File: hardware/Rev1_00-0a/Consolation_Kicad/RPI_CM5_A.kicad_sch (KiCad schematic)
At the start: 61 parts, among them J17 61300311121, J19 RPI_CMx_A, J7 2998TR, Q17 2N7002, Q19 SSM3K56FS,LF, Q20 SSM3K56FS,LF, Q21 SSM3K56FS,LF, Q22 SSM3K56FS,LF, U19 SN74LVC1G125DBVR, U21 MCP7940NT-I/MS, Y2 32.768kHz

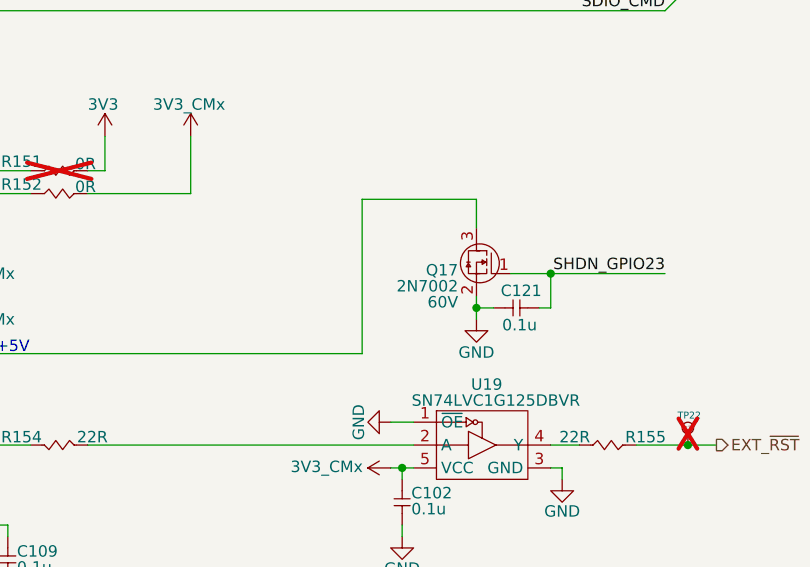
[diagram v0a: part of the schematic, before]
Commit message: Removed unnecessary functions (USB2 mux, CapTouch) Adjusted 220uF alum capacitor for codec (slimmer version)
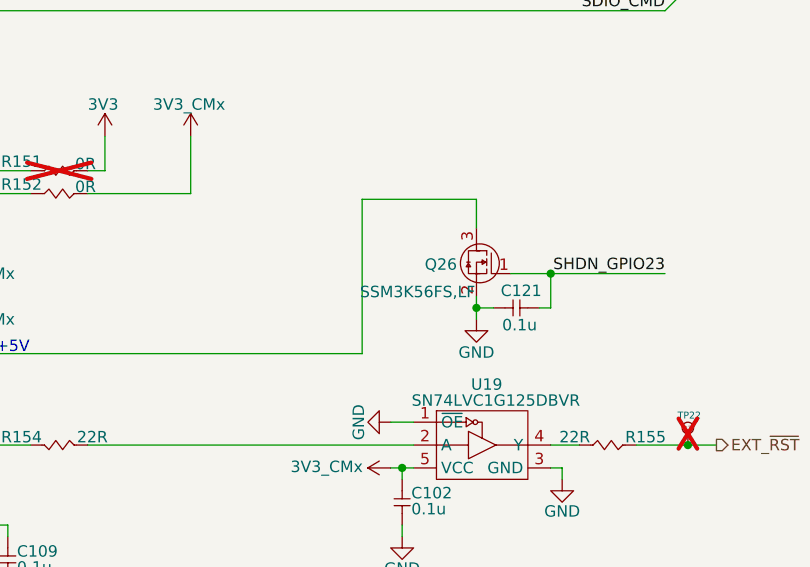
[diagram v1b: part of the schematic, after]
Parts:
- removed Q17: 2N7002, footprint:SOT-23-3, symbol KicadCompDb:Mosfet/MOSFET_00001
- added Q26: SSM3K56FS,LF, footprint:SC-75, symbol KicadCompDb:Mosfet/MOSFET_00002
- J7: footprint 2998TR -> footprint:2998TR; Package (none) -> 6.8MM
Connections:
- net GND: now also Q26.2 (S)
- net SHDN_GPIO23: now also Q26.1 (G)
- net at J19.92 (RUN_PG/PWR_BTN): now also Q26.3 (D)
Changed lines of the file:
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@@
 			)
 		)
-		(property "Footprint" "2998TR"
+		(property "Footprint" "footprint:2998TR"
 			(at 87.63 193.675 0)
 			(hide yes)
@@
 			)
 		)
+		(property "Package" "6.8MM"
+			(at 87.63 193.675 0)
+			(hide yes)
+			(show_name no)
+			(do_not_autoplace no)
+			(effects
+				(font
+					(size 1.27 1.27)
+				)
+			)
+		)
 		(pin "2"
 		)
@@
 	)
 	(symbol
-		(lib_id "KicadCompDb:Mosfet/MOSFET_00001")
-		(at 251.46 122.555 0)
-		(mirror y)
-		(unit 1)
-		(body_style 1)
-		(exclude_from_sim no)
-		(in_bom yes)
-		(on_board yes)
-		(in_pos_files yes)
-		(dnp no)
-		(property "Reference" "Q17"
-			(at 245.618 122.174 0)
-			(show_name no)
-			(do_not_autoplace no)
-			(effects
-				(font
-					(size 1.27 1.27)
-				)
-				(justify left)
-			)
-		)
-		(property "Value" "2N7002"
-			(at 245.618 123.952 0)
-			(show_name no)
-			(do_not_autoplace no)
-			(effects
-				(font
-					(size 1.27 1.27)
-				)
-				(justify left)
-			)
-		)
-		(property "Footprint" "footprint:SOT-23-3"
-			(at 251.46 122.555 0)
-			(hide yes)
-			(show_name no)
-			(do_not_autoplace no)
-			(effects
-				(font
-					(size 1.27 1.27)
-				)
-			)
-		)
-		(property "Datasheet" "https://www.diodes.com/assets/Datasheets/ds11303.pdf"
-			(at 251.46 122.555 0)
-			(hide yes)
-			(show_name no)
-			(do_not_autoplace no)
-			(effects
-				(font
-					(size 1.27 1.27)
-				)
-			)
-		)
-		(property "Description" "MOSFET N-CH 60V 115MA SOT23-3"
-			(at 251.46 122.555 0)
-			(hide yes)
-			(show_name no)
-			(do_not_autoplace no)
-			(effects
-				(font
-					(size 1.27 1.27)
-				)
-			)
-		)
-		(property "VDS" "60V"
-			(at 245.618 125.73 0)
-			(show_name no)
-			(do_not_autoplace no)
-			(effects
-				(font
-					(size 1.27 1.27)
-				)
-				(justify left)
-			)
-		)
-		(property "Package" "SOT-23-3"
-			(at 251.46 122.555 0)
-			(hide yes)
-			(show_name no)
-			(do_not_autoplace no)
-			(effects
-				(font
-					(size 1.27 1.27)
-				)
-			)
-		)
-		(property "Type" "NFET"
-			(at 251.46 122.555 0)
-			(hide yes)
-			(show_name yes)
-			(do_not_autoplace no)
-			(effects
-				(font
-					(size 1.27 1.27)
-				)
-			)
-		)
-		(property "I(drain)" "0.115A"
-			(at 251.46 122.555 0)
-			(hide yes)
-			(show_name yes)
-			(do_not_autoplace no)
-			(effects
-				(font
-					(size 1.27 1.27)
-				)
-			)
-		)
-		(property "VGS(th)" "2.5V"
-			(at 251.46 122.555 0)
-			(hide yes)
-			(show_name yes)
-			(do_not_autoplace no)
-			(effects
-				(font
-					(size 1.27 1.27)
-				)
-			)
-		)
-		(property "RDS(on)" "7.5Ohm"
-			(at 251.46 122.555 0)
-			(hide yes)
-			(show_name yes)
-			(do_not_autoplace no)
-			(effects
-				(font
-					(size 1.27 1.27)
-				)
-			)
-		)
-		(property "Power" "0.37W"
-			(at 251.46 122.555 0)
-			(hide yes)
-			(show_name yes)
-			(do_not_autoplace no)
-			(effects
-				(font
-					(size 1.27 1.27)
-				)
-			)
-		)
-		(property "Operating Temperature" "-55°C ~ 150°C"
-			(at 251.46 122.555 0)
-			(hide yes)
-			(show_name yes)
-			(do_not_autoplace no)
-			(effects
-				(font
-					(size 1.27 1.27)
-				)
-			)
-		)
-		(property "Dimensions" "2.90mm x 2.40mm"
-			(at 251.46 122.555 0)
-			(hide yes)
-			(show_name yes)
-			(do_not_autoplace no)
-			(effects
-				(font
-					(size 1.27 1.27)
-				)
-			)
-		)
-		(property "Manufacturer" "Diodes Incorporated"
-			(at 251.46 122.555 0)
-			(hide yes)
-			(show_name yes)
-			(do_not_autoplace no)
-			(effects
-				(font
-					(size 1.27 1.27)
-				)
-			)
-		)
-		(property "Manufacturer Part Number" "2N7002-7-F"
-			(at 251.46 122.555 0)
-			(hide yes)
-			(show_name yes)
-			(do_not_autoplace no)
-			(effects
-				(font
-					(size 1.27 1.27)
-				)
-			)
-		)
-		(property "Distributor" "DigiKey"
-			(at 251.46 122.555 0)
-			(hide yes)
-			(show_name yes)
-			(do_not_autoplace no)
-			(effects
-				(font
-					(size 1.27 1.27)
-				)
-			)
-		)
-		(property "Distributor Part Number" "2N7002-FDICT-ND"
-			(at 251.46 122.555 0)
-			(hide yes)
-			(show_name yes)
-			(do_not_autoplace no)
-			(effects
-				(font
-					(size 1.27 1.27)
-				)
-			)
-		)
-		(pin "1"
-		)
-		(pin "3"
-		)
-		(pin "2"
-		)
-		(instances
-			(project "Consolation_Kicad"
-				(path "/b18b5a64-cfe0-4447-acaf-556f3c6e6513/75d0c21e-3f51-4c04-91a3-13b7a2863fa1"
-					(reference "Q17")
-					(unit 1)
-				)
-			)
-		)
-	)
-	(symbol
 		(lib_id "KicadCompDb:Resistors/RES_SMT_00016")
 		(at 80.01 191.135 180)
@@
 					(unit 1)
 				)
+			)
+		)
+	)
+	(symbol
+		(lib_id "KicadCompDb:Mosfet/MOSFET_00002")
+		(at 251.46 122.555 0)
+		(mirror y)
+		(unit 1)
+		(body_style 1)
+		(exclude_from_sim no)
+		(in_bom yes)
+		(on_board yes)
+		(in_pos_files yes)
+		(dnp no)
+		(property "Reference" "Q26"
+			(at 245.491 121.539 0)
+			(show_name no)
+			(do_not_autoplace no)
+			(effects
+				(font
+					(size 1.27 1.27)
+				)
+				(justify left)
+			)
+		)
+		(property "Value" "SSM3K56FS,LF"
+			(at 247.523 124.587 0)
+			(show_name no)
+			(do_not_autoplace no)
+			(effects
+				(font
+					(size 1.27 1.27)
+				)
+				(justify left)
+			)
+		)
+		(property "Footprint" "footprint:SC-75"
+			(at 251.46 122.555 0)
+			(hide yes)
+			(show_name no)
+			(do_not_autoplace no)
+			(effects
+				(font
+					(size 1.27 1.27)
+				)
+			)
+		)
+		(property "Datasheet" "https://toshiba.semicon-storage.com/info/docget.jsp?did=13419&prodName=SSM3K56FS"
+			(at 251.46 122.555 0)
+			(hide yes)
+			(show_name no)
+			(do_not_autoplace no)
+			(effects
+				(font
+					(size 1.27 1.27)
+				)
+			)
+		)
+		(property "Description" "MOSFET N-CH 20V 800MA SSM"
+			(at 251.46 122.555 0)
+			(hide yes)
+			(show_name no)
+			(do_not_autoplace no)
+			(effects
+				(font
+					(size 1.27 1.27)
+				)
+			)
+		)
+		(property "Operating Temperature" "-55°C ~ 150°C"
+			(at 251.46 122.555 0)
+			(hide yes)
+			(show_name yes)
+			(do_not_autoplace no)
+			(effects
+				(font
+					(size 1.27 1.27)
+				)
+			)
+		)
+		(property "Power" "0.15W"
+			(at 251.46 122.555 0)
+			(hide yes)
+			(show_name yes)
+			(do_not_autoplace no)
+			(effects
+				(font
+					(size 1.27 1.27)
+				)
+			)
+		)
+		(property "RDS(on)" "0.235Ohm"
+			(at 251.46 122.555 0)
+			(hide yes)
+			(show_name yes)
+			(do_not_autoplace no)
+			(effects
+				(font
+					(size 1.27 1.27)
+				)
+			)
+		)
+		(property "I(drain)" "0.8A"
+			(at 251.46 122.555 0)
+			(hide yes)
+			(show_name yes)
+			(do_not_autoplace no)
+			(effects
+				(font
+					(size 1.27 1.27)
+				)
+			)
+		)
+		(property "Dimensions" "1.60mm x 1.60mm"
+			(at 251.46 122.555 0)
+			(hide yes)
+			(show_name yes)
+			(do_not_autoplace no)
+			(effects
+				(font
+					(size 1.27 1.27)
+				)
+			)
+		)
+		(property "VGS(th)" "1V"
+			(at 251.46 122.555 0)
+			(hide yes)
+			(show_name yes)
+			(do_not_autoplace no)
+			(effects
+				(font
+					(size 1.27 1.27)
+				)
+			)
+		)
+		(property "Distributor Part Number" "264-SSM3K56FS,LFCT-ND"
+			(at 251.46 122.555 0)
+			(hide yes)
+			(show_name yes)
+			(do_not_autoplace no)
+			(effects
+				(font
+					(size 1.27 1.27)
+				)
+			)
+		)
+		(property "Distributor" "DigiKey"
+			(at 251.46 122.555 0)
+			(hide yes)
+			(show_name yes)
+			(do_not_autoplace no)
+			(effects
+				(font
+					(size 1.27 1.27)
+				)
+			)
+		)
+		(property "Type" "NFET"
+			(at 251.46 122.555 0)
+			(hide yes)
+			(show_name yes)
+			(do_not_autoplace no)
+			(effects
+				(font
+					(size 1.27 1.27)
+				)
+			)
+		)
+		(property "Manufacturer Part Number" "SSM3K56FS,LF"
+			(at 251.46 122.555 0)
+			(hide yes)
+			(show_name yes)
+			(do_not_autoplace no)
+			(effects
+				(font
+					(size 1.27 1.27)
+				)
+			)
+		)
+		(property "Manufacturer" "Toshiba Semiconductor and Storage"
+			(at 251.46 122.555 0)
+			(hide yes)
+			(show_name yes)
+			(do_not_autoplace no)
+			(effects
+				(font
+					(size 1.27 1.27)
+				)
+			)
+		)
+		(property "VDS" "20V"
+			(at 245.618 123.825 0)
+			(hide yes)
+			(show_name no)
+			(do_not_autoplace no)
+			(effects
+				(font
+					(size 1.27 1.27)
+				)
+				(justify left)
+			)
+		)
+		(property "Package" "SC-75"
+			(at 251.46 122.555 0)
+			(hide yes)
+			(show_name no)
+			(do_not_autoplace no)
+			(effects
+				(font
+					(size 1.27 1.27)
+				)
+			)
+		)
+		(pin "2"
+		)
+		(pin "3"
+		)
+		(pin "1"
+		)
+		(instances
+			(project "Consolation_Kicad"
+				(path "/b18b5a64-cfe0-4447-acaf-556f3c6e6513/75d0c21e-3f51-4c04-91a3-13b7a2863fa1"
+					(reference "Q26")
+					(unit 1)
+				)

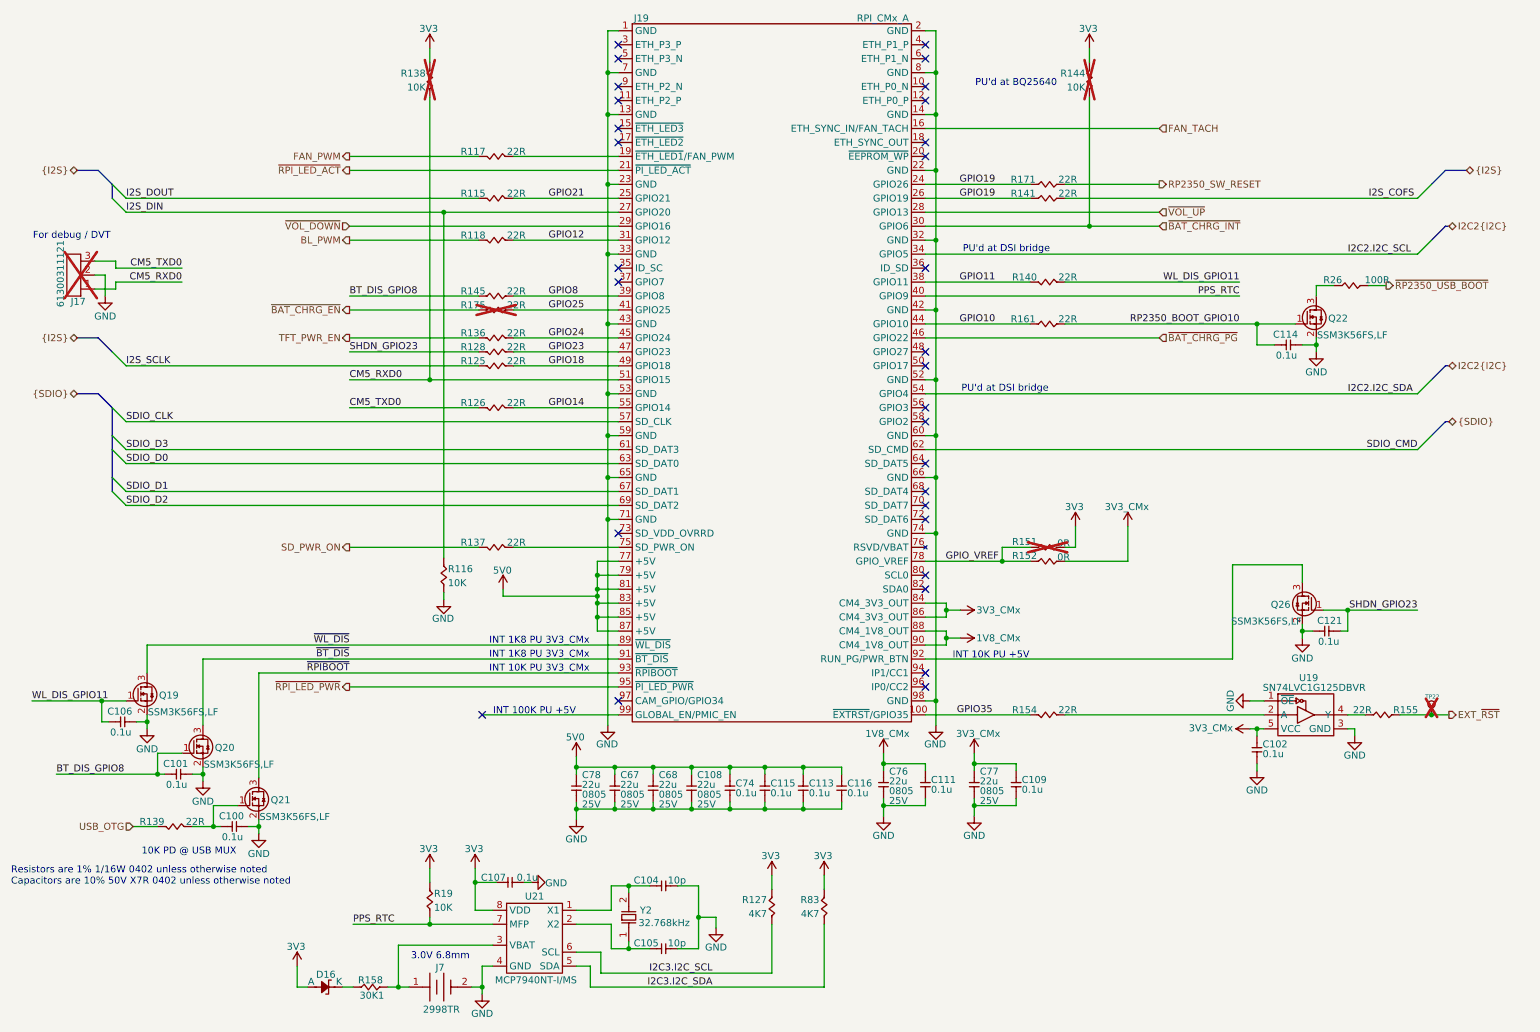
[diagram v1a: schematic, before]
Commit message: Component preliminary placement
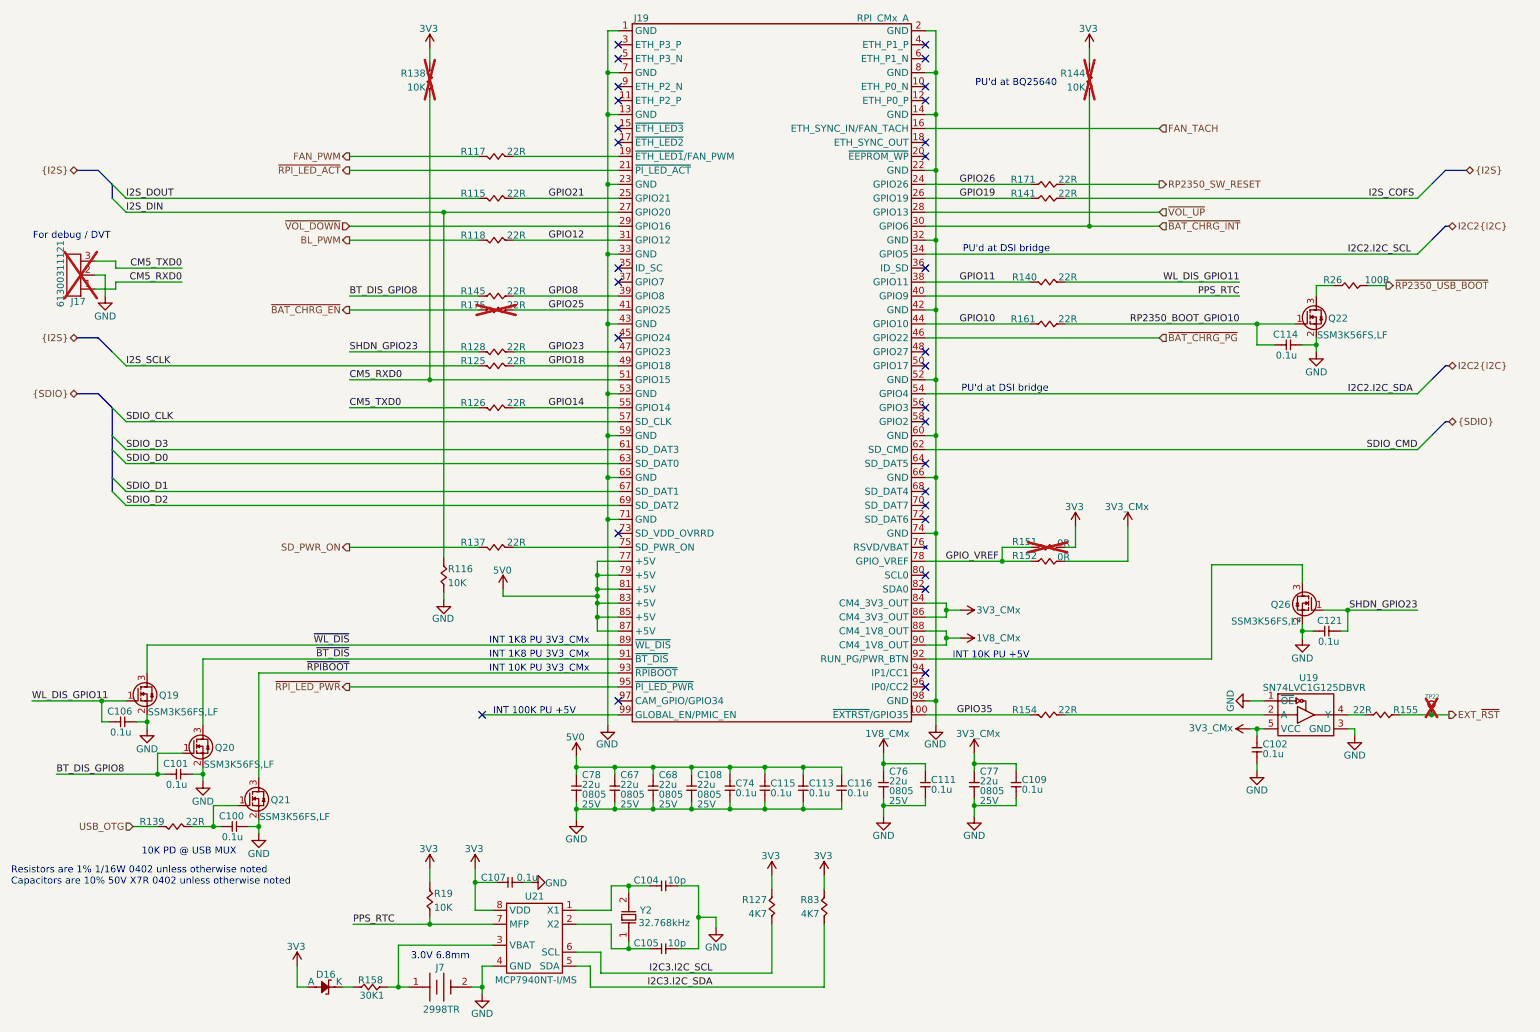
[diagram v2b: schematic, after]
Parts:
- removed R136: 22R, footprint:RES_0402, symbol KicadCompDb:Resistors/RES_SMT_00015
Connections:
- net GPIO19: no longer J19.24 (GPIO26), R171.1
- net GPIO24: no longer names the net of J19.45 (GPIO24)
- new net GPIO26: J19.24 (GPIO26), R171.1
- no-connect marks 30 -> 31

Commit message: Preliminary placement of Consolation continues
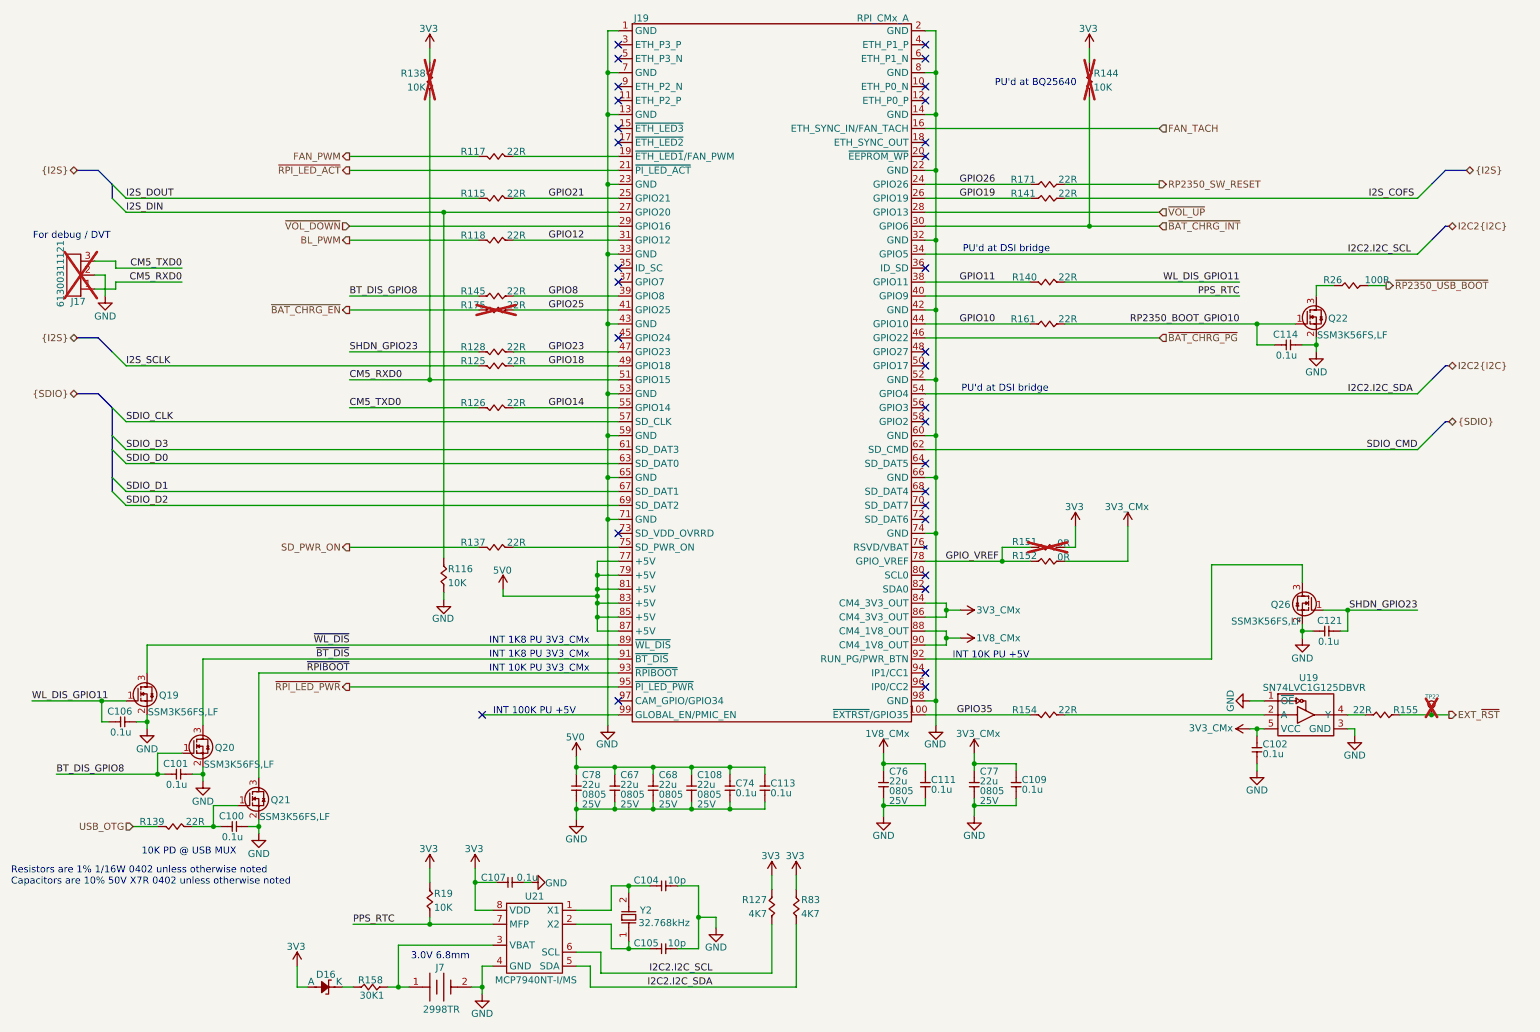
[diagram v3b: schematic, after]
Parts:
- removed C115, C116: 0.1u, footprint:CAP_NONPOL_0402, symbol KicadCompDb:Capacitors/CAP_CER_SMT_00001
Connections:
- net I2C3.I2C_SCL is gone; now on net I2C2.I2C_SCL: R127.1, U21.6 (SCL)
- net I2C3.I2C_SDA is gone; now on net I2C2.I2C_SDA: R83.1, U21.5 (SDA)
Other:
- moved on the sheet: C113, R144, R83
